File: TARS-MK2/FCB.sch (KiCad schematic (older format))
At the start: 31 parts, among them J101 505567-0681, J102 505567-0681, J103 505567-0681, J104 505567-0681, J105 505578-0671, J106 505578-0671, U101 LSM9DS1, U102 KX122-1711, U103 MS5611-01BA, U104 MPU-9250, U105 ublox_SAM-M8Q, U106 RFM95W-915S2, X101 SMA

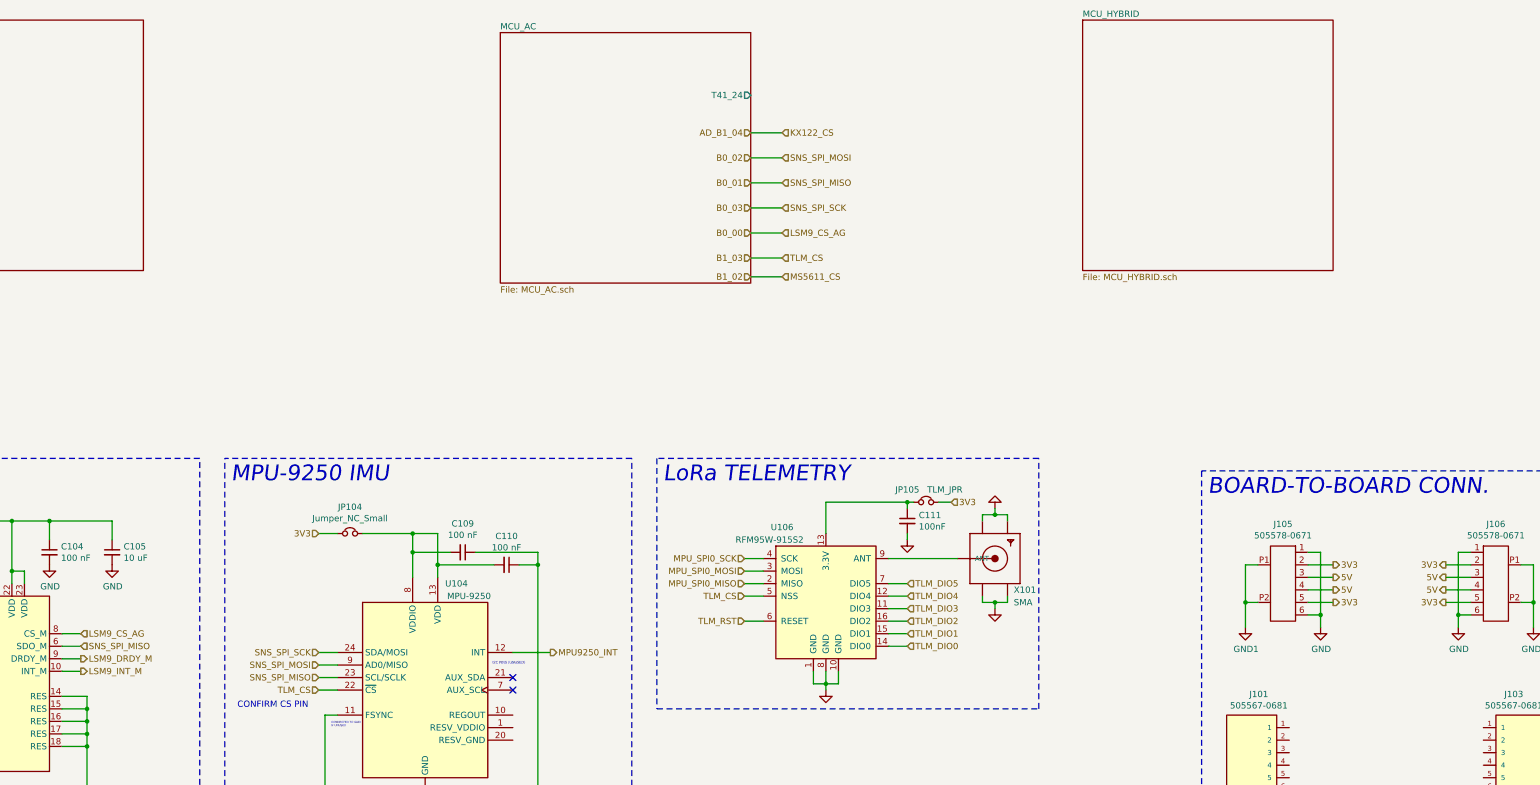
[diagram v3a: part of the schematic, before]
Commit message: added traces to FCB board
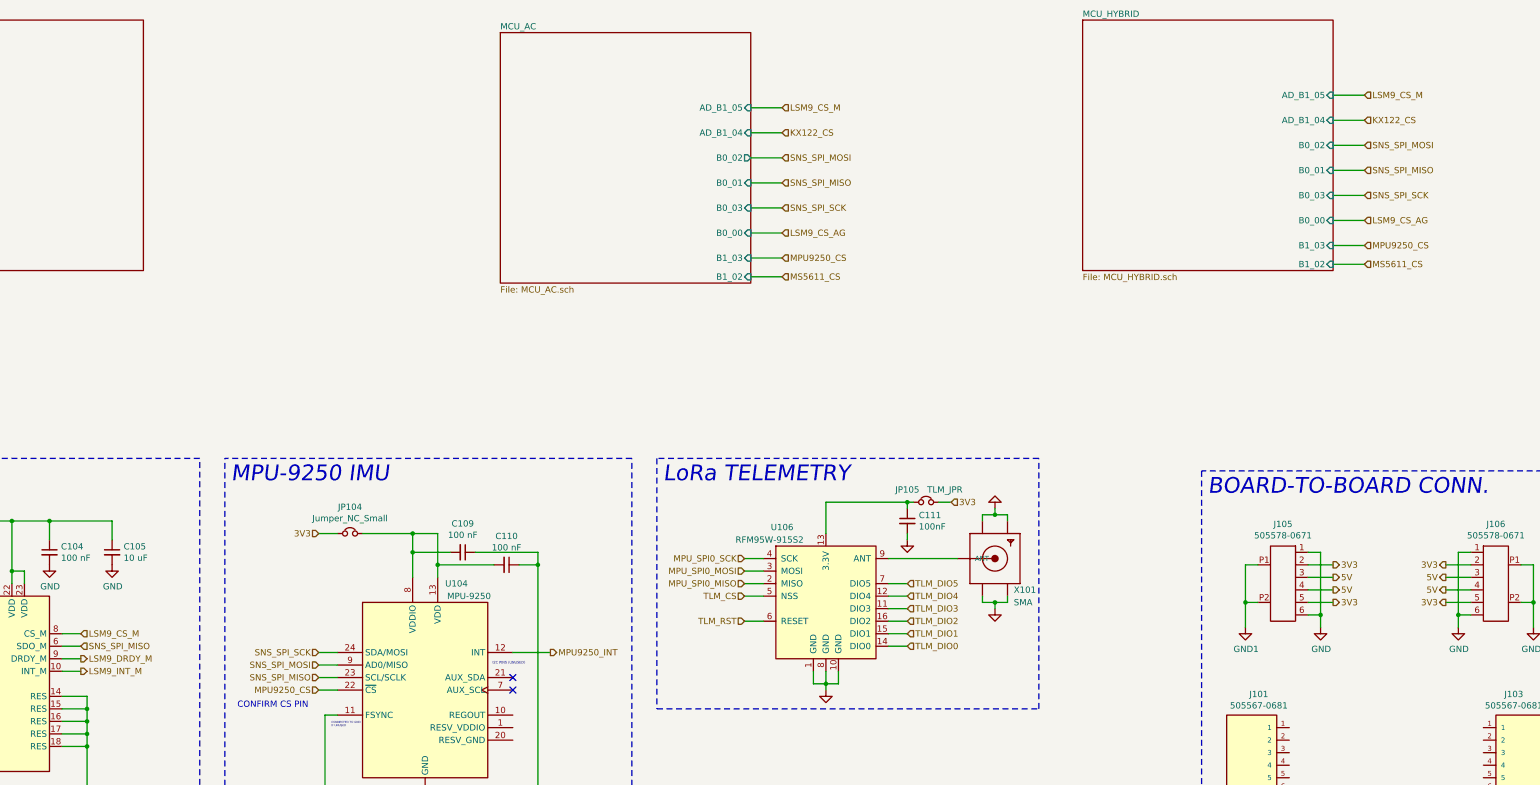
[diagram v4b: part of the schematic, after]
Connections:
- net AD_B1_04 renamed KX122_CS
- net B0_00 renamed LSM9_CS_AG
- net LSM9_CS_AG: no longer U101.8 (CS_M)
- net B0_01 renamed SNS_SPI_MISO
- net B0_02 renamed SNS_SPI_MOSI
- net B0_03 renamed SNS_SPI_SCK
- net B1_02 renamed MS5611_CS
- net B1_03 renamed MPU9250_CS
- net MPU9250_CS: no longer U106.5 (NSS)
- new net LSM9_CS_M: U101.8 (CS_M)
- new net TLM_CS: U106.5 (NSS)
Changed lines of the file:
@@
 F0 "MCU_HYBRID" 50
 F1 "MCU_HYBRID.sch" 50
-$EndSheet
-$Sheet
-S 7250 1550 2000 2000
-U 60021F5A
-F0 "MCU_AC" 50
-F1 "MCU_AC.sch" 50
-F2 "T41_24" O R 9250 2050 50
+F2 "AD_B1_04" I R 13900 2250 50
+F3 "B0_02" I R 13900 2450 50
+F4 "B0_01" I R 13900 2650 50
+F5 "B0_03" I R 13900 2850 50
+F6 "B0_00" I R 13900 3050 50
+F7 "B1_03" I R 13900 3250 50
+F8 "B1_02" I R 13900 3400 50
+F9 "AD_B1_05" I R 13900 2050 50
 $EndSheet
 $Comp
@@
 Text HLabel 5800 6700 0    50   Input ~ 0
 SNS_SPI_MISO
-Text HLabel 5800 6800 0    50   Input ~ 0
-TLM_CS
 Wire Wire Line
 	5800 6500 5950 6500
@@
 	2200 6750 2350 6750
 Text HLabel 3900 6350 2    50   Input ~ 0
-LSM9_CS_AG
+LSM9_CS_M
 Wire Wire Line
 	3750 6350 3900 6350
@@
 Text HLabel 6000 9900 2    50   Output ~ 0
 KX122_INT2
-Text HLabel 9250 2550 0    50   Input ~ 0
-B0_02
+Text HLabel 9500 2950 2    50   Input ~ 0
+SNS_SPI_SCK
+Wire Wire Line
+	9250 2950 9500 2950
+Text HLabel 9500 3150 2    50   Input ~ 0
+LSM9_CS_AG
+Wire Wire Line
+	9250 3150 9500 3150
+Wire Wire Line
+	9250 3350 9500 3350
+Text HLabel 9500 3500 2    50   Input ~ 0
+MS5611_CS
+Wire Wire Line
+	9250 3500 9500 3500
+Text HLabel 9500 2350 2    50   Input ~ 0
+KX122_CS
+Wire Wire Line
+	9250 2350 9500 2350
 Text HLabel 9500 2550 2    50   Input ~ 0
 SNS_SPI_MOSI
 Wire Wire Line
-	9250 2550 9500 2550
-Text HLabel 9250 2750 0    50   Input ~ 0
-B0_01
+	9500 2550 9250 2550
 Text HLabel 9500 2750 2    50   Input ~ 0
 SNS_SPI_MISO
 Wire Wire Line
 	9250 2750 9500 2750
-Text HLabel 9250 2950 0    50   Input ~ 0
-B0_03
-Text HLabel 9500 2950 2    50   Input ~ 0
+Text HLabel 14150 2850 2    50   Input ~ 0
 SNS_SPI_SCK
 Wire Wire Line
-	9250 2950 9500 2950
-Text HLabel 9250 3150 0    50   Input ~ 0
-B0_00
-Text HLabel 9500 3150 2    50   Input ~ 0
+	13900 2850 14150 2850
+Text HLabel 14150 3050 2    50   Input ~ 0
 LSM9_CS_AG
 Wire Wire Line
-	9250 3150 9500 3150
-Text HLabel 9250 3350 0    50   Input ~ 0
-B1_03
+	13900 3050 14150 3050
+Text HLabel 14150 3250 2    50   Input ~ 0
+MPU9250_CS
+Wire Wire Line
+	13900 3250 14150 3250
+Text HLabel 14150 3400 2    50   Input ~ 0
+MS5611_CS
+Wire Wire Line
+	13900 3400 14150 3400
+Text HLabel 14150 2250 2    50   Input ~ 0
+KX122_CS
+Wire Wire Line
+	13900 2250 14150 2250
+Text HLabel 14150 2450 2    50   Input ~ 0
+SNS_SPI_MOSI
+Wire Wire Line
+	14150 2450 13900 2450
+Text HLabel 14150 2650 2    50   Input ~ 0
+SNS_SPI_MISO
+Wire Wire Line
+	13900 2650 14150 2650
 Text HLabel 9500 3350 2    50   Input ~ 0
-TLM_CS
-Wire Wire Line
-	9250 3350 9500 3350
-Text HLabel 9250 3500 0    50   Input ~ 0
-B1_02
-Text HLabel 9500 3500 2    50   Input ~ 0
-MS5611_CS
-Wire Wire Line
-	9250 3500 9500 3500
-Text HLabel 9250 2350 0    50   Input ~ 0
-AD_B1_04
-Text HLabel 9500 2350 2    50   Input ~ 0
-KX122_CS
-Wire Wire Line
-	9250 2350 9500 2350
+MPU9250_CS
+Text HLabel 5800 6800 0    50   Input ~ 0
+MPU9250_CS
+Text HLabel 9500 2150 2    50   Input ~ 0
+LSM9_CS_M
+$Sheet
+S 7250 1550 2000 2000
+U 60021F5A
+F0 "MCU_AC" 50
+F1 "MCU_AC.sch" 50
+F2 "B0_02" O R 9250 2550 50
+F3 "B0_01" I R 9250 2750 50
+F4 "B0_03" I R 9250 2950 50
+F5 "B0_00" I R 9250 3150 50
+F6 "B1_02" I R 9250 3500 50
+F7 "B1_03" I R 9250 3350 50
+F8 "AD_B1_04" I R 9250 2350 50
+F9 "AD_B1_05" I R 9250 2150 50
+$EndSheet
+Wire Wire Line
+	9500 2150 9250 2150
+Text HLabel 14150 2050 2    50   Input ~ 0
+LSM9_CS_M
+Wire Wire Line
+	14150 2050 13900 2050
 $EndSCHEMATC

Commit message: MPU crystal + grounding + SYSBOOT tweaks
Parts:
- C111: footprint (none) -> Capacitor_SMD:C_0603_1608Metric
- X101: footprint (none) -> SMA_connector:SMA90_DIP
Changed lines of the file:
@@
 F 0 "C111" H 10592 5496 50  0000 L CNN
 F 1 "100nF" H 10592 5405 50  0000 L CNN
-F 2 "" H 10500 5450 50  0001 C CNN
+F 2 "Capacitor_SMD:C_0603_1608Metric" H 10500 5450 50  0001 C CNN
 F 3 "~" H 10500 5450 50  0001 C CNN
 	1    10500 5450
@@
 F 0 "X101" H 11350 5500 50  0000 L CNN
 F 1 "SMA" H 11350 5400 50  0000 L CNN
-F 2 "" H 11200 5750 50  0001 C CNN
+F 2 "SMA_connector:SMA90_DIP" H 11200 5750 50  0001 C CNN
 F 3 "" H 11200 5750 50  0001 C CNN
 	1    11200 5750

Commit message: Broke out MCU communication buses
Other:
- note added: "(connectors n stuff)"
- note added: "Board-2-Board I2C Bus\n (T41 I2C0)"
- note added: "INTERFACING"
- note added: "MCU - MPU SPI BUS\n [MCU IS SLAVE]\n (T41 SPI1)"
- note added: "MCU_AC - MCU_HYB UART\n (T41 UART2)"
- note added: "MCU_AC - MPU UART\n (T41 UART1)"
- note added: "MCU_HYB - MPU UART\n (T41 UART1)"
- note added: "MISCELLANEOUS"
- note added: "MOLEX MLPlus\n1.25mm 6pos"
- note added: "MOLEX MLPlus\n2.00mm 6pos"
- note added: "MPU STUFFS"
- note added: "SENSOR SUITE SPI BUS\n (T41 SPI0)"
- note added: "SNESORS"
- note added: "{"
- note added: "}"
- moved on the sheet: C101, C102, C103, C104, C105, C106, C107, C108, C109, C110, C111, J101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

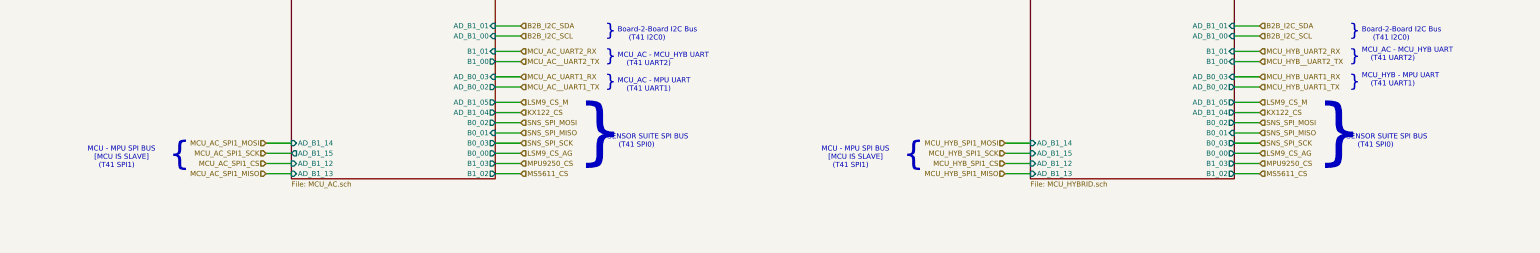
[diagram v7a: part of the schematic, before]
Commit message: Allocated LPSPI2 to B2B SPI bus, found SPI mapping of SNS_SPI and MPU-MCU SPI busses
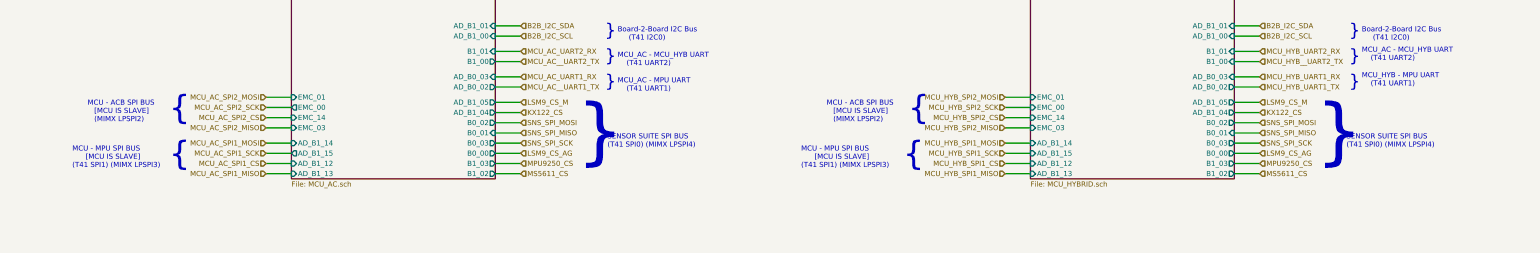
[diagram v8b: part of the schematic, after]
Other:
- note added: "MCU - ACB SPI BUS\n [MCU IS SLAVE]\n (MIMX LPSPI2)"
- note added: "MCU - MPU SPI BUS\n [MCU IS SLAVE]\n(T41 SPI1) (MIMX LPSPI3)"
- note added: "SENSOR SUITE SPI BUS\n(T41 SPI0) (MIMX LPSPI4)"
- note removed: "MCU - MPU SPI BUS\n [MCU IS SLAVE]\n (T41 SPI1)"
- note removed: "SENSOR SUITE SPI BUS\n (T41 SPI0)"
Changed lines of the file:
@@
 $EndComp
 $Comp
-L power:GND1 #PWR0102
+L FCB-rescue:GND1-power #PWR0102
 U 1 1 6116E3F0
 P 21900 14200
@@
 F18 "AD_B1_00" I R 19200 3500 50
 F19 "AD_B1_01" I R 19200 3400 50
+F20 "EMC_03" I L 17200 4400 50
+F21 "EMC_14" I L 17200 4300 50
+F22 "EMC_00" I L 17200 4200 50
+F23 "EMC_01" I L 17200 4100 50
 $EndSheet
 $Comp
@@
 	11300 10700 11300 10650
 $Comp
-L power:GND1 #PWR0146
+L FCB-rescue:GND1-power #PWR0146
 U 1 1 607DE6C1
 P 14200 9800
@@
 	14200 9650 14200 9350
 $Comp
-L power:GND1 #PWR0147
+L FCB-rescue:GND1-power #PWR0147
 U 1 1 607F3B40
 P 16500 9800
@@
 3V3
 $Comp
-L power:GND1 #PWR0150
+L FCB-rescue:GND1-power #PWR0150
 U 1 1 60870BB0
 P 16000 12450
@@
 	14650 11000 14650 11100
 $Comp
-L power:GND1 #PWR0151
+L FCB-rescue:GND1-power #PWR0151
 U 1 1 608B1F0E
 P 14650 12450
@@
 }
 Text Notes 13050 4600 0    50   ~ 0
-SENSOR SUITE SPI BUS\n     (T41 SPI0)
-Text Notes 20300 4600 0    50   ~ 0
-SENSOR SUITE SPI BUS\n     (T41 SPI0)
+ SENSOR SUITE SPI BUS\n(T41 SPI0) (MIMX LPSPI4)
 Text Notes 3750 8050 0    315  Italic 0
 SNESORS
@@
 F18 "AD_B1_00" I R 11950 3500 50
 F19 "AD_B1_01" I R 11950 3400 50
+F20 "EMC_03" I L 9950 4400 50
+F21 "EMC_14" I L 9950 4300 50
+F22 "EMC_00" O L 9950 4200 50
+F23 "EMC_01" I L 9950 4100 50
 $EndSheet
 Text HLabel 12200 3750 2    50   Input ~ 0
@@
 Wire Wire Line
 	17200 4850 16950 4850
-Text Notes 7950 4800 0    50   ~ 0
-MCU - MPU SPI BUS\n   [MCU IS SLAVE]\n     (T41 SPI1)
+Text Notes 7800 4800 0    50   ~ 0
+   MCU - MPU SPI BUS\n      [MCU IS SLAVE]\n(T41 SPI1) (MIMX LPSPI3)
 Text Notes 8750 4800 0    236  ~ 0
 {
-Text Notes 15150 4800 0    50   ~ 0
-MCU - MPU SPI BUS\n   [MCU IS SLAVE]\n     (T41 SPI1)
 Text Notes 15950 4800 0    236  ~ 0
 {
@@
 Text Notes 20450 3550 0    50   ~ 0
 Board-2-Board I2C Bus\n     (T41 I2C0)
+Text Notes 14950 4800 0    50   ~ 0
+   MCU - MPU SPI BUS\n      [MCU IS SLAVE]\n(T41 SPI1) (MIMX LPSPI3)
+Text Notes 20300 4600 0    50   ~ 0
+ SENSOR SUITE SPI BUS\n(T41 SPI0) (MIMX LPSPI4)
+Text HLabel 9700 4100 0    50   Input ~ 0
+MCU_AC_SPI2_MOSI
+Wire Wire Line
+	9950 4100 9700 4100
+Text HLabel 9700 4200 0    50   Input ~ 0
+MCU_AC_SPI2_SCK
+Wire Wire Line
+	9950 4200 9700 4200
+Text HLabel 9700 4300 0    50   Input ~ 0
+MCU_AC_SPI2_CS
+Wire Wire Line
+	9950 4300 9700 4300
+Text HLabel 9700 4400 0    50   Input ~ 0
+MCU_AC_SPI2_MISO
+Wire Wire Line
+	9950 4400 9700 4400
+Text Notes 7950 4350 0    50   ~ 0
+MCU - ACB SPI BUS\n   [MCU IS SLAVE]\n   (MIMX LPSPI2)
+Text Notes 8750 4350 0    236  ~ 0
+{
+Text HLabel 16950 4100 0    50   Input ~ 0
+MCU_HYB_SPI2_MOSI
+Wire Wire Line
+	17200 4100 16950 4100
+Text HLabel 16950 4200 0    50   Input ~ 0
+MCU_HYB_SPI2_SCK
+Wire Wire Line
+	17200 4200 16950 4200
+Text HLabel 16950 4300 0    50   Input ~ 0
+MCU_HYB_SPI2_CS
+Wire Wire Line
+	17200 4300 16950 4300
+Text HLabel 16950 4400 0    50   Input ~ 0
+MCU_HYB_SPI2_MISO
+Wire Wire Line
+	17200 4400 16950 4400
+Text Notes 16000 4350 0    236  ~ 0
+{
+Text Notes 15200 4350 0    50   ~ 0
+MCU - ACB SPI BUS\n   [MCU IS SLAVE]\n   (MIMX LPSPI2)
 $EndSCHEMATC
